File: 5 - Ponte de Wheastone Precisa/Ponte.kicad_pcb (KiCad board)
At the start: 2 copper layers, 84.9 x 39.3 mm, 20 parts, among them J1 Conn_01x02, J3 Conn_01x02, J4 Conn_01x02, J5 Conn_01x02, Q1 MMBT2222A, Q2 MMBT2222A, U1 LM358, U2 INA333, U3 LM385D-2.5

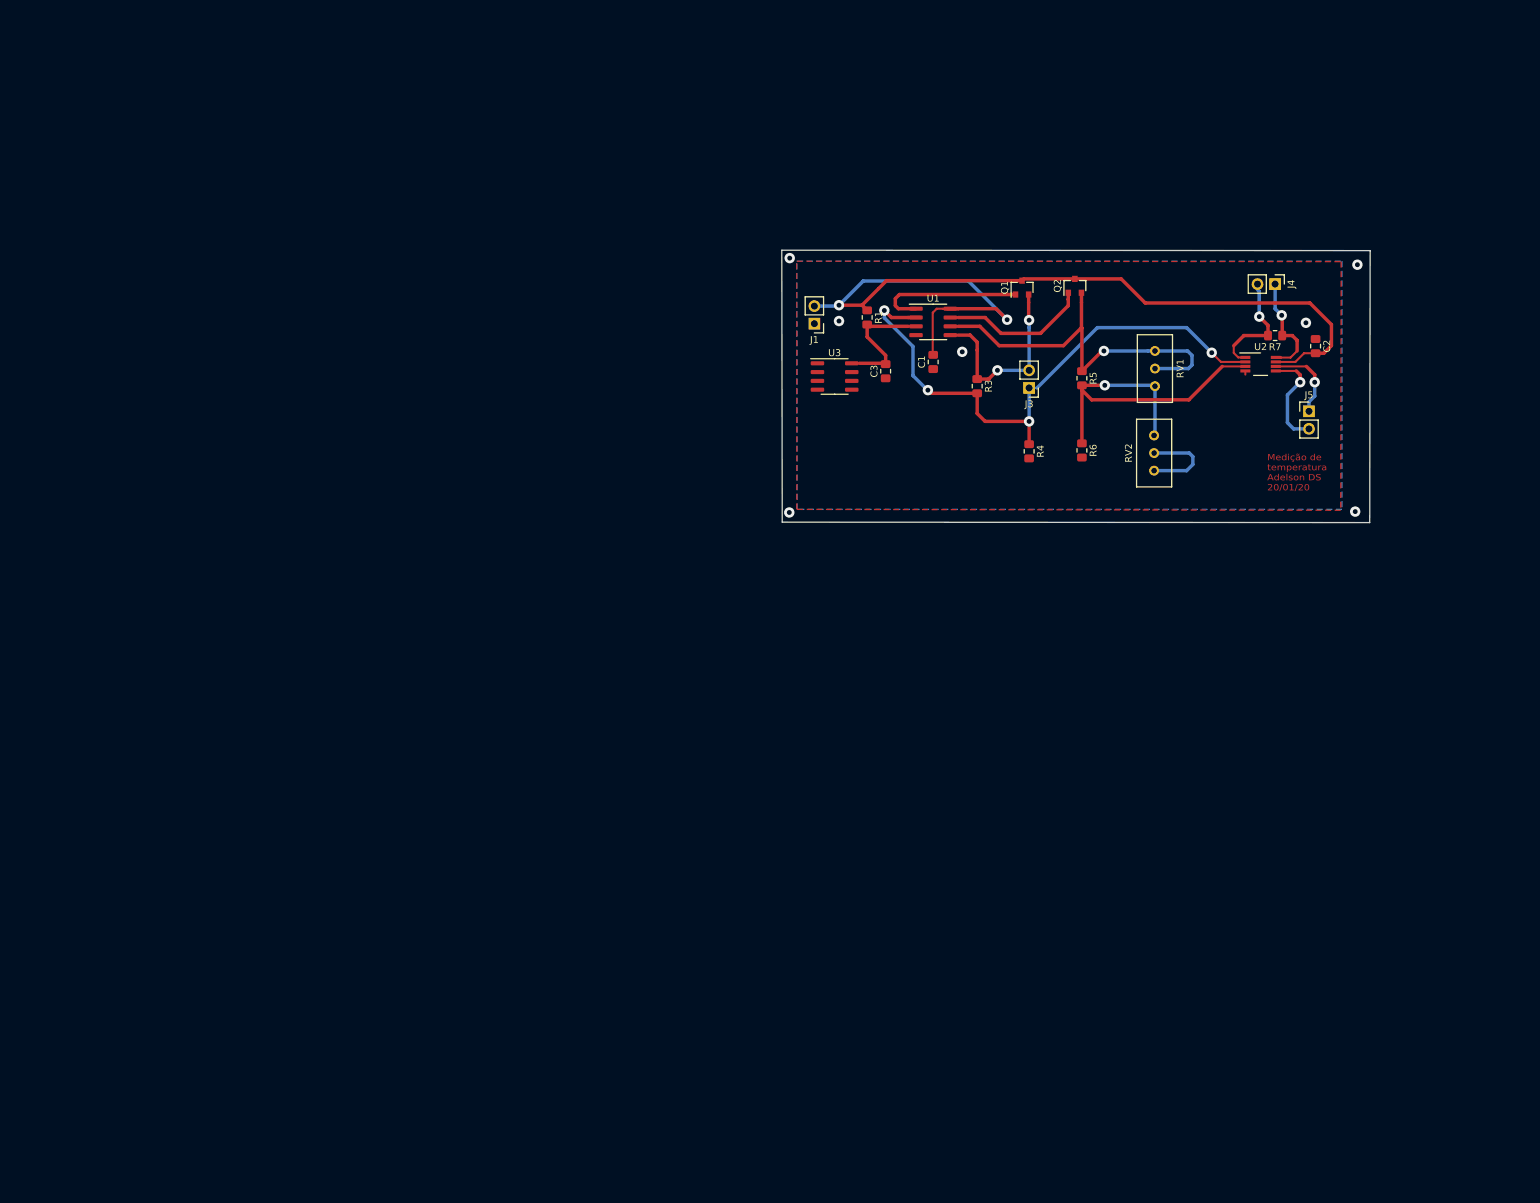
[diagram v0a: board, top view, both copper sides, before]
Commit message: Adicionado sensor 4 fios; PCB_1
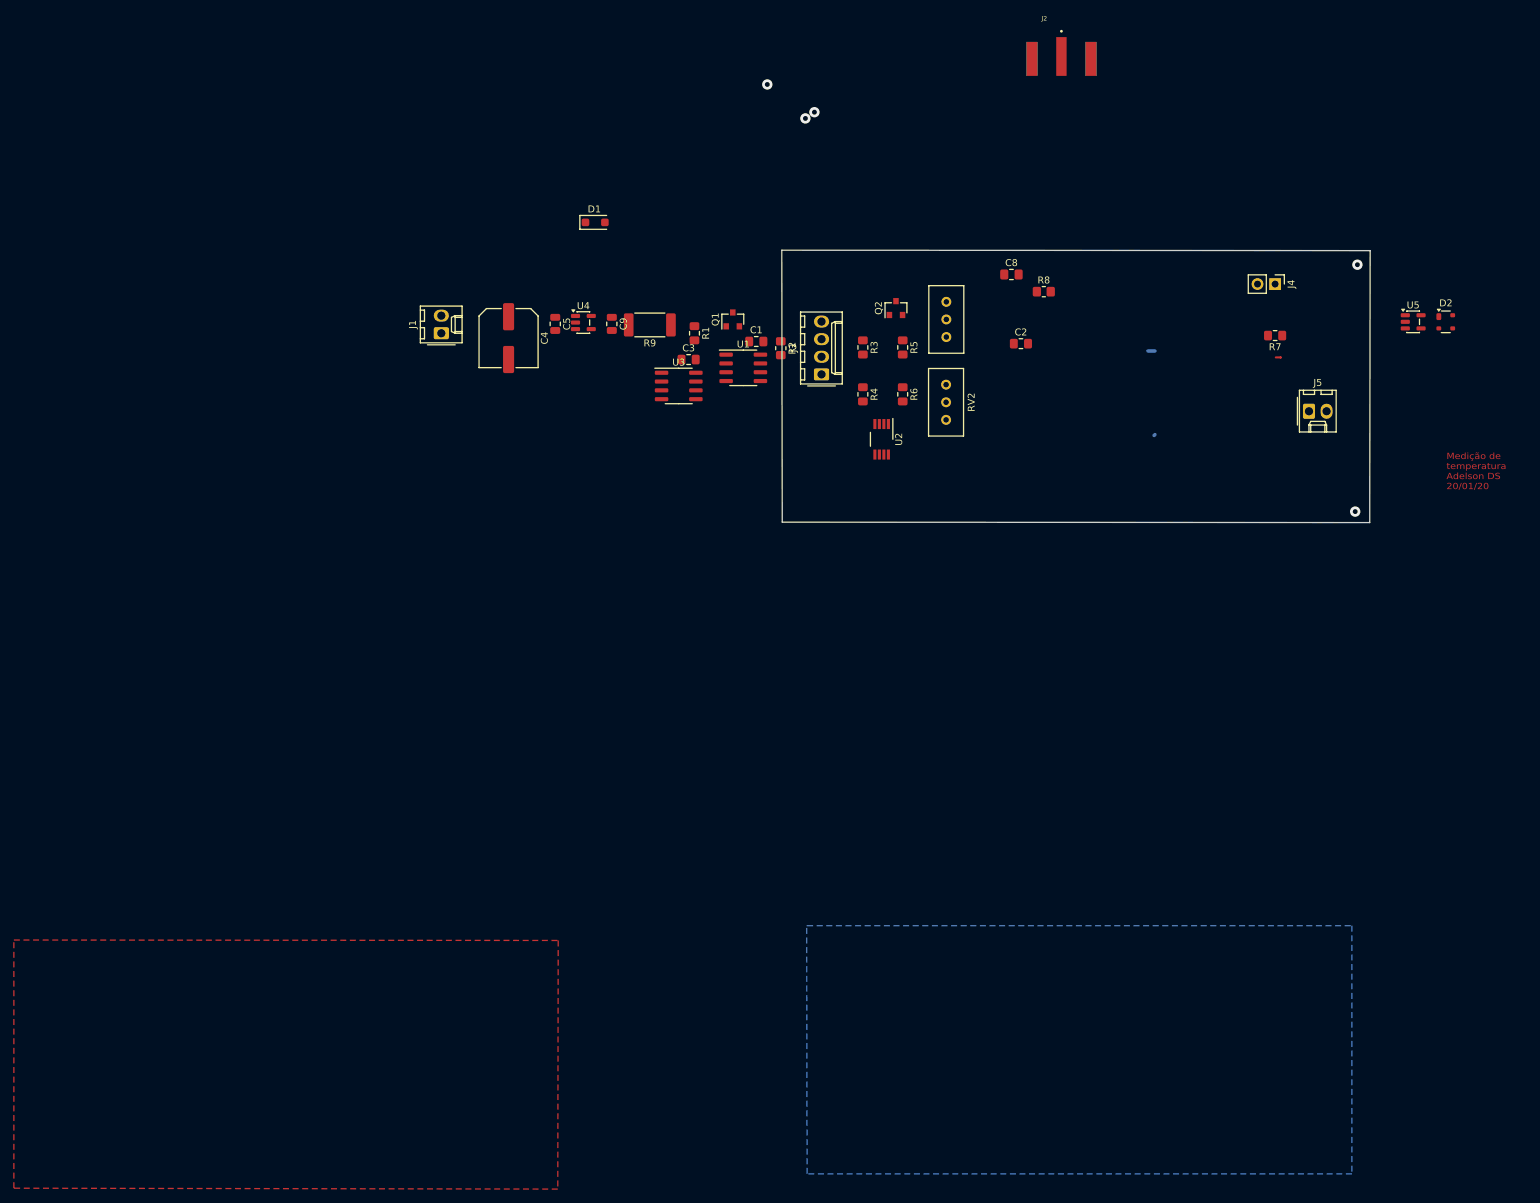
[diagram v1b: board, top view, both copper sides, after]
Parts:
- added C4: 100uF, Capacitor_SMD:C_Elec_8x6.2, F.Cu at (55.4, 129.0)
- added C5: 4.7uF, Capacitor_SMD:C_0805_2012Metric, F.Cu at (62.2, 126.9)
- added C8: 0.1uF, Capacitor_SMD:C_0805_2012Metric_Pad1.18x1.45mm_HandSolder, F.Cu at (128.0, 119.8)
- added C9: 4.7uF, Capacitor_SMD:C_0805_2012Metric, F.Cu at (70.3, 126.9)
- added D1: SMF13A, Diode_SMD:D_SOD-123F, F.Cu at (67.9, 112.3)
- added D2: PRTR5V0U2X, Package_TO_SOT_SMD:SOT-143, F.Cu at (190.7, 126.6)
- added J2: V_OUT, CONSMA020.062-G:LINX_CONSMA020.062-G, F.Cu at (135.2, 91.1)
- added R2: 10, Resistor_SMD:R_0805_2012Metric_Pad1.20x1.40mm_HandSolder, F.Cu at (94.7, 130.4)
- added R8: 10, Resistor_SMD:R_0805_2012Metric_Pad1.20x1.40mm_HandSolder, F.Cu at (132.7, 122.3)
- added R9: 1, Resistor_SMD:R_2512_6332Metric_Pad1.40x3.35mm_HandSolder, F.Cu at (75.8, 127.1)
- added U4: TPS709B50DBVR, Package_TO_SOT_SMD:SOT-23-5, F.Cu at (66.2, 126.7)
- added U5: TI OPA192IDBVR, Package_TO_SOT_SMD:SOT-23-5, F.Cu at (186.0, 126.6)
- C1: value 10nF -> 0.1uF
- J1: value Conn_01x02 -> Supply; footprint Connector_PinHeader_2.54mm:PinHeader_1x02_P2.54mm_Vertical -> Connector_Molex:Molex_KK-254_AE-6410-02A_1x02_P2.54mm_Vertical
- J3: value Conn_01x02 -> Sensor; footprint Connector_PinHeader_2.54mm:PinHeader_1x02_P2.54mm_Vertical -> Connector_Molex:Molex_KK-254_AE-6410-04A_1x04_P2.54mm_Vertical
- J4: value Conn_01x02 -> R_adj
- J5: value Conn_01x02 -> V_OUT; footprint Connector_PinHeader_2.54mm:PinHeader_1x02_P2.54mm_Vertical -> Connector_Molex:Molex_KK-254_AE-6410-02A_1x02_P2.54mm_Vertical
- R1: value 250k -> 120k
- R4, R6: value 250 -> 240
- R5: value 8 -> 8.2
- U1: value LM358 -> OPA2192IDR
- U3: value LM385D-2.5 -> LM285D-2.5R2G
- moved U2 55.7 mm to (109.3, 143.6), turned to -90 degrees
- moved J1 53.8 mm to (45.7, 128.3), turned to 90 degrees
- moved C2 42.5 mm to (129.4, 129.8), turned to 0 degrees
- moved Q1 42.0 mm to (87.8, 126.3)
- moved RV1 30.9 mm to (118.6, 128.8)
- moved RV2 30.1 mm to (118.6, 140.8), turned to -90 degrees
- moved J3 30.0 mm to (100.6, 134.2), turned to 90 degrees
- moved C3 28.5 mm to (81.4, 132.0), turned to 0 degrees
- moved U1 28.2 mm to (89.3, 133.2)
- moved R6 27.1 mm to (112.3, 137.1)
- moved R5 26.2 mm to (112.3, 130.3)
- moved Q2 26.0 mm to (111.3, 124.6)
- moved C1 25.7 mm to (91.2, 129.4), turned to 0 degrees
- moved R4 25.4 mm to (106.6, 137.1)
- moved R1 25.0 mm to (82.3, 128.3)
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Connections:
- J1 pad 2: +5V -> Net-(D1-A1)
- J3 pad 1: Net-(J3-Pad1) -> Net-(J3-Pin_1)
- J3 pad 2: Net-(J3-Pad2) -> /S-
- J5 pad 1: Net-(J5-Pad1) -> Net-(J5-Pin_1)
- J5 pad 2: Net-(J5-Pad2) -> GND
- Q1 pad 2: Net-(J3-Pad2) -> Net-(J3-Pin_4)
- Q2 pad 1: Net-(Q2-Pad1) -> Net-(Q2-B)
- R3 pad 1: Net-(J3-Pad2) -> Net-(J3-Pin_4)
- R3 pad 2: Net-(J3-Pad1) -> Net-(J3-Pin_1)
- R4 pad 1: Net-(J3-Pad1) -> Net-(J3-Pin_1)
- R5 pad 2: Net-(R5-Pad2) -> /S+
- R6 pad 1: Net-(R5-Pad2) -> /S+
- RV1 pad 1: Net-(R5-Pad2) -> /S+
- RV2 pad 1: Net-(R5-Pad2) -> GND
- RV2 pad 3: GND -> /S+
- U1 pad 2: Net-(J3-Pad1) -> Net-(J3-Pin_1)
- U1 pad 5: Net-(J3-Pad2) -> Net-(J3-Pin_3)
- U1 pad 7: Net-(Q2-Pad1) -> Net-(R2-Pad2)
- U2 pad 2: Net-(J3-Pad1) -> /S-
- U2 pad 3: Net-(R5-Pad2) -> /S+
- U2 pad 5: Net-(J5-Pad2) -> GND
- U2 pad 6: Net-(J5-Pad1) -> Net-(R8-Pad1)
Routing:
- net +5V: track 139.1 -> 0.00 mm, vias 2 -> 0
- net Net-(J3-Pad1): track 82.8 -> 0.00 mm, vias 4 -> 0
- net Net-(Q2-E): track 56.6 -> 1.02 mm, vias 1 -> 0
- net Net-(R5-Pad2): track 53.0 -> 0.00 mm, vias 1 -> 0
- net Net-(J3-Pad2): track 28.8 -> 0.00 mm, vias 2 -> 0
- net Net-(Q1-B): track 21.8 -> 0.00 mm
- net Net-(Q2-Pad1): track 21.5 -> 0.00 mm
- net +2V5: track 18.9 -> 0.00 mm
- net Net-(J4-Pin_2): track 15.8 -> 0.00 mm, vias 1 -> 0
- net Net-(J5-Pad2): track 14.9 -> 0.00 mm, vias 1 -> 0
- net Net-(J4-Pin_1): track 14.5 -> 0.73 mm, vias 1 -> 0
- net GND: track 13.4 -> 0.00 mm, vias 3 -> 0
- net Net-(J5-Pad1): track 11.7 -> 0.00 mm, vias 1 -> 0
- net /S-: vias 0 -> 1
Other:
- copper layers 2 -> 4
- board text added: "Conector de Alimentação (VCC / GND) Posicionar próximo ao regulador ou fonte, longe dos sensores Rastros de alimentação largos (mínimo 1,0 mm para até 1 A) em L4 Via stitching entre L3 (plano PWR) e o pad do conector para baixa impedância Capacitor bulk 10-47 µF (tantalum ou eletrolítico de baixo ESR) na entrada do conector Capacitor cerâmico 100 nF o mais próximo possível do conector Ferrite bea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"
- board text added: "Conector de Sinal de Saída (Vout analógico ou digital) Saída analógica (tensão/corrente) Buffer de saída obrigatório (ex: OPA227, AD8605) - nunca conectar a saída do amp de instrumentação diretamente ao conector sem buffer Resistor de isolamento de carga (10-100 Ω) em série na saída antes do conector, para estabilidade com cargas capacitivas de cabos longos Capacitor 100 pF entre a saída e GND no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"
- board text added: "Conector dos Sensores Resistivos (Strain Gauge / Termistor / Potenciômetro) É o conector mais crítico do projeto - qualquer ruído aqui compromete toda a medição. Para ambientes com vibração: Lemo 00 ou Fischer (travamento por rosca) Para bancada/lab: Phoenix Contact ou blocos de parafuso com proteção contra vibração Evitar terminais simples de pino sem trava em aplicações industriais Entrar o cab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"
- board text added: "LAYER 1 - Sinal + componentes Posicionamento dos resistores de strain gauge ou sensores da ponte Rastros de sinal diferencial da ponte com impedância controlada (~100 Ω diff) Manter rastros curtos e simétricos entre os 4 braços da pont"
- board text added: "LAYER 2 - GND Analógico (plano contínuo) Plano de terra ininterrupto sob toda a área analógica Referência de retorno imediata para L1 → baixa indutância de loop Separar fisicamente (split plane) se houver porção digital no mesmo board É a camada mais crítica para CMRR (Rejeição de Modo Comum)"
- board text added: "LAYER 3 - Alimentação / GND Digital Plano de VCC para os amplificadores de instrumentação (ex: INA128, AD8221) Se o circuito for 100% analógico: usar como segundo plano GND para blindagem Desacoplar referências de tensão (REF) aqui com capacitores de 100 nF+10 µF"
- board text added: "LAYER 4 - Sinal Rastros de alimentação bulk, conectores, comunicação de saída Pode conter blindagem adicional (hatched copper pour ligado a GND) Evitar roteamento de sinais sensíveis nesta camada"
- board text added: "RECOMENDAÇÕES"
- board text added: "Simetria de rastros: os 4 braços da ponte devem ter comprimento e largura idênticos para minimizar offset termal Par diferencial: o sinal de saída da ponte (Vout+ e Vout−) deve ser roteado como par diferencial em L1, com distância constante e sem vias desnecessárias Guard ring: circundar os nós de alta impedância com anel de guarda conectado a GND analógico em L2 Desacoplamento local: capacitores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"

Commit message: Posicionado e roteado. Restando adicionar vias de GND e guard ring.
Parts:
- added C6: 100pF, Capacitor_SMD:C_0805_2012Metric_Pad1.18x1.45mm_HandSolder, F.Cu at (128.9, 119.7)
- added C7: 100pF, Capacitor_SMD:C_0805_2012Metric_Pad1.18x1.45mm_HandSolder, F.Cu at (130.1, 130.5)
- added D3: LED, LED_SMD:LED_0805_2012Metric, F.Cu at (44.1, 133.1)
- added R10: 2.2k, Resistor_SMD:R_0805_2012Metric, F.Cu at (68.5, 133.6)
- added R11: 10, Resistor_SMD:R_0805_2012Metric_Pad1.20x1.40mm_HandSolder, F.Cu at (127.4, 130.5)
- added R12: 2.2k, Resistor_SMD:R_0805_2012Metric, F.Cu at (64.3, 130.0)
- J4: footprint Connector_PinHeader_2.54mm:PinHeader_1x02_P2.54mm_Vertical -> Connector_Molex:Molex_KK-254_AE-6410-02A_1x02_P2.54mm_Vertical
- moved D2 87.7 mm to (103.1, 131.3), turned to -90 degrees
- moved U5 62.1 mm to (124.0, 130.6)
- moved R7 51.7 mm to (114.4, 127.4)
- moved J4 50.4 mm to (115.7, 121.3), turned to 180 degrees
- moved J5 42.2 mm to (134.3, 118.6), turned to -90 degrees
- moved J2 38.4 mm to (137.7, 129.4), turned to 90 degrees
- moved Q2 29.3 mm to (87.5, 141.6), turned to 180 degrees
- moved D1 25.2 mm to (47.9, 127.5), turned to -90 degrees
- moved RV1 22.9 mm to (97.1, 136.8), turned to 90 degrees
- moved R4 22.0 mm to (86.4, 128.3), turned to 90 degrees
- moved R8 16.1 mm to (119.9, 132.1)
- moved R2 16.0 mm to (83.1, 141.4), turned to 90 degrees
- moved U2 13.8 mm to (114.3, 130.7), turned to 0 degrees
- moved R5 12.6 mm to (102.1, 137.7), turned to 90 degrees
- moved R3 11.8 mm to (96.9, 123.6)
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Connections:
- C4 pad 1: Net-(D1-A1) -> +VIN
- C5 pad 1: Net-(D1-A1) -> +VIN
- D1 pad 1: Net-(D1-A1) -> +VIN
- J1 pad 2: Net-(D1-A1) -> +VIN
- RV2 pad 1: GND -> /S+
- RV2 pad 3: /S+ -> GND
- U4 pad 1: Net-(D1-A1) -> +VIN
- U4 pad 3: Net-(D1-A1) -> Net-(U4-EN)
- U5 pad 1: Net-(J5-Pin_1) -> Net-(U5--)
- U5 pad 4: Net-(J5-Pin_1) -> Net-(U5--)
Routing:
- net Net-(J3-Pin_1): track 0.00 -> 38.7 mm, vias 0 -> 1
- net /S+: track 0.18 -> 29.9 mm
- net Net-(J3-Pin_4): track 0.00 -> 28.4 mm
- net +VIN: track 0.00 -> 27.8 mm, vias 0 -> 10
- net Net-(D3-A): track 0.00 -> 25.3 mm
- net Net-(J5-Pin_1): track 0.00 -> 25.0 mm
- net Net-(J3-Pin_3): track 0.00 -> 24.9 mm
- net Net-(Q2-E): track 1.02 -> 25.4 mm
- net /S-: track 0.00 -> 20.2 mm
- net +5V: track 0.00 -> 18.1 mm, vias 0 -> 28
- net +2V5: track 0.00 -> 11.6 mm
- net Net-(J4-Pin_2): track 0.00 -> 8.99 mm
- net Net-(J4-Pin_1): track 0.73 -> 8.91 mm
- net Net-(R2-Pad2): track 0.00 -> 6.81 mm
- net Net-(Q1-B): track 0.00 -> 6.71 mm
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- added copper zone on F.Cu, net +5V
- added copper zone on In2.Cu, net +5V
- added copper zone on In2.Cu, net +VIN
- added copper zone on In1.Cu, net GND
- removed copper zone on B.Cu, net GND
- removed copper zone on F.Cu, net GND
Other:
- board size 84.9 x 39.3 mm -> 100 x 35 mm

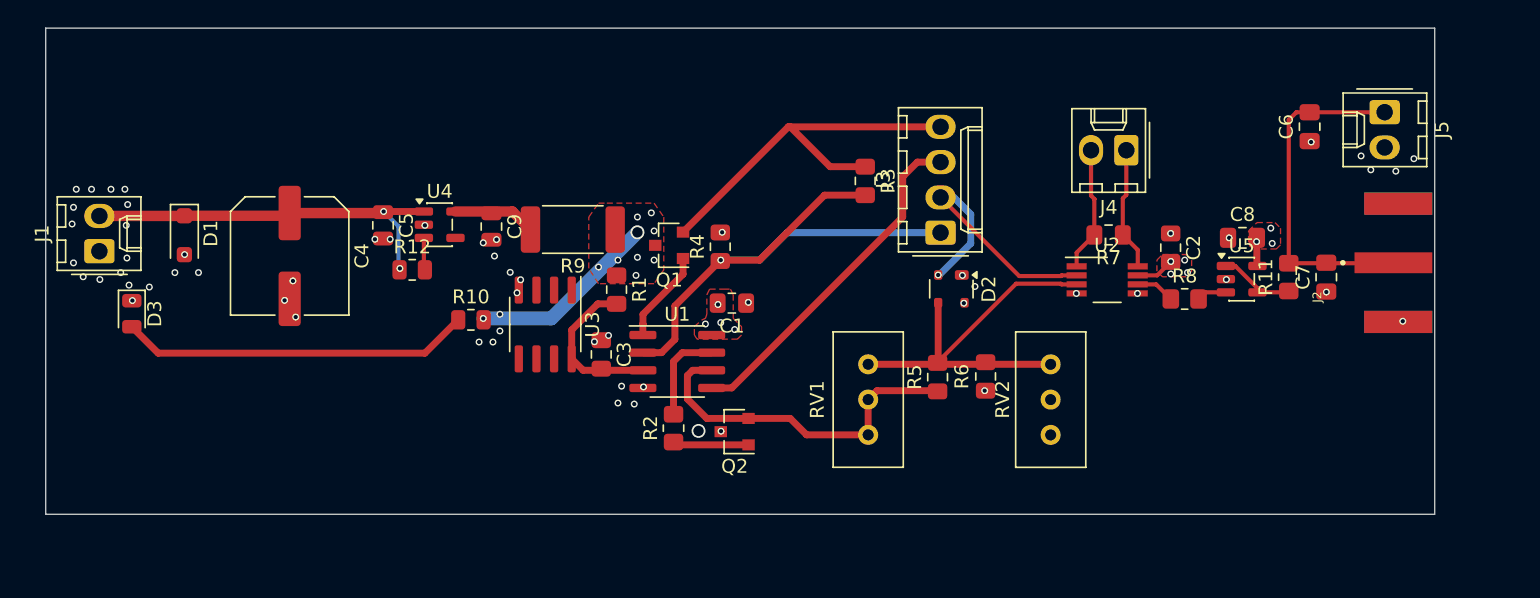
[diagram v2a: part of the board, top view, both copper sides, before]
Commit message: Adicionado silks e furos para suporte. Preço com montagem R04,54
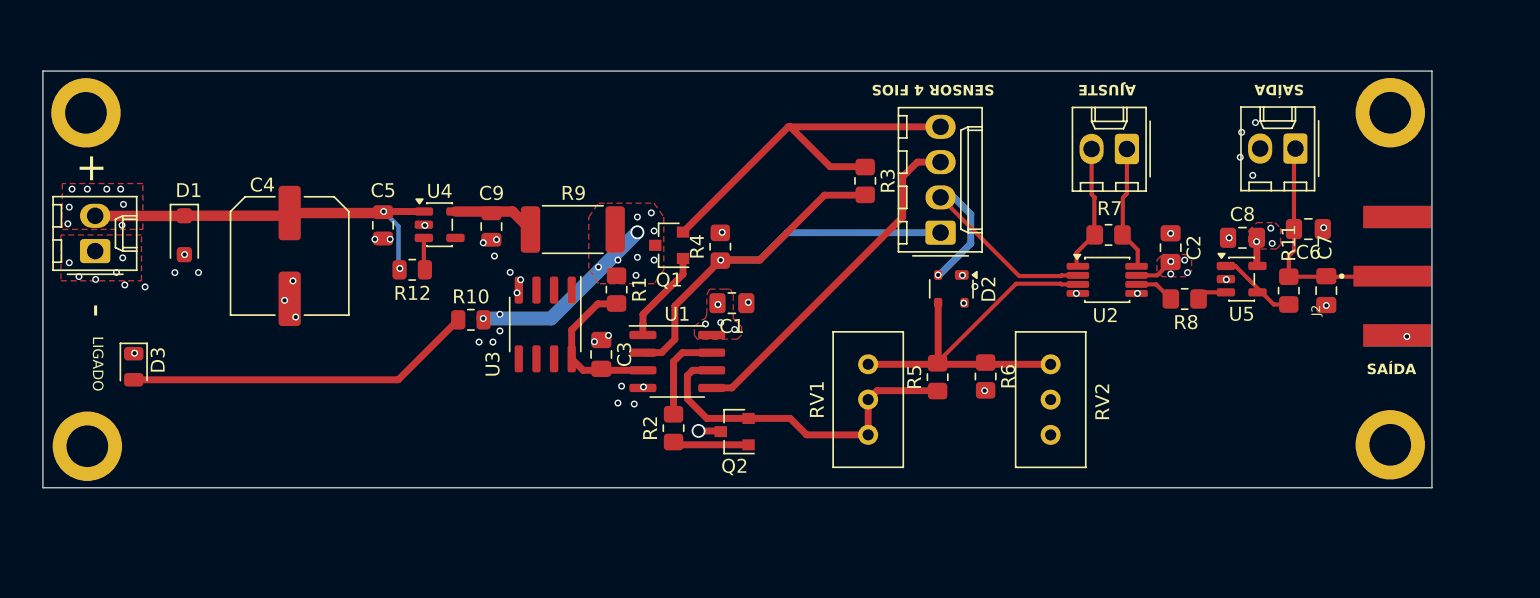
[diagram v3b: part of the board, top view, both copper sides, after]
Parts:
- added ?: , , F.Cu at (137.7, 115.7)
- added ?: , , F.Cu at (40.9, 118.7)
- added ?: , , F.Cu at (134.7, 118.6)
- added ?: , , F.Cu at (134.8, 118.7)
- C1, C2, C3: footprint Capacitor_SMD:C_0805_2012Metric_Pad1.15x1.40mm_HandSolder -> Capacitor_SMD:C_0805_2012Metric_Pad1.18x1.45mm_HandSolder
- R1, R3, R4, R5, R6, R7: footprint Resistor_SMD:R_0805_2012Metric_Pad1.15x1.40mm_HandSolder -> Resistor_SMD:R_0805_2012Metric_Pad1.20x1.40mm_HandSolder
- U2: footprint Package_SO:VSSOP-8_3.0x3.0mm_P0.65mm -> Package_SO:VSSOP-8_3x3mm_P0.65mm
- moved C6 7.37 mm to (128.8, 127.0), turned to 180 degrees
- moved J5 6.94 mm to (127.8, 121.2), turned to 180 degrees
- moved D3 3.82 mm to (44.2, 136.9)
- moved J2 0.97 mm to (137.6, 130.4)
- moved C7 0.97 mm to (130.1, 131.5)
- moved R11 0.97 mm to (127.4, 131.5)
- moved J1 0.30 mm to (41.4, 128.6)
- moved J4 0.10 mm to (115.7, 121.3)
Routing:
- net Net-(J5-Pin_1): track 25.0 -> 16.9 mm
- net +5V: track 18.1 -> 19.8 mm, vias 28 -> 27
- added copper zone on F.Cu, net +VIN
- added copper zone on F.Cu, net GND
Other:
- board size 100 x 35 mm -> 100 x 30 mm
- board text added: "+"
- board text added: "-"
- board text added: "AJUSTE"
- board text added: "LIGADO"
- board text added: "SAÍDA"
- board text added: "SENSOR 4 FIOS"
